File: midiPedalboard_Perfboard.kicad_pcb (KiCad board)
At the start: 4 copper layers, 66 x 50.8 mm, 53 parts, among them J1 wire, J10 wire, J11 wire, J12 wire, J13 wire, J14 wire, J15 MIDI_4, J16 MIDI_5, J17 MIDI_4, J18 MIDI_2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

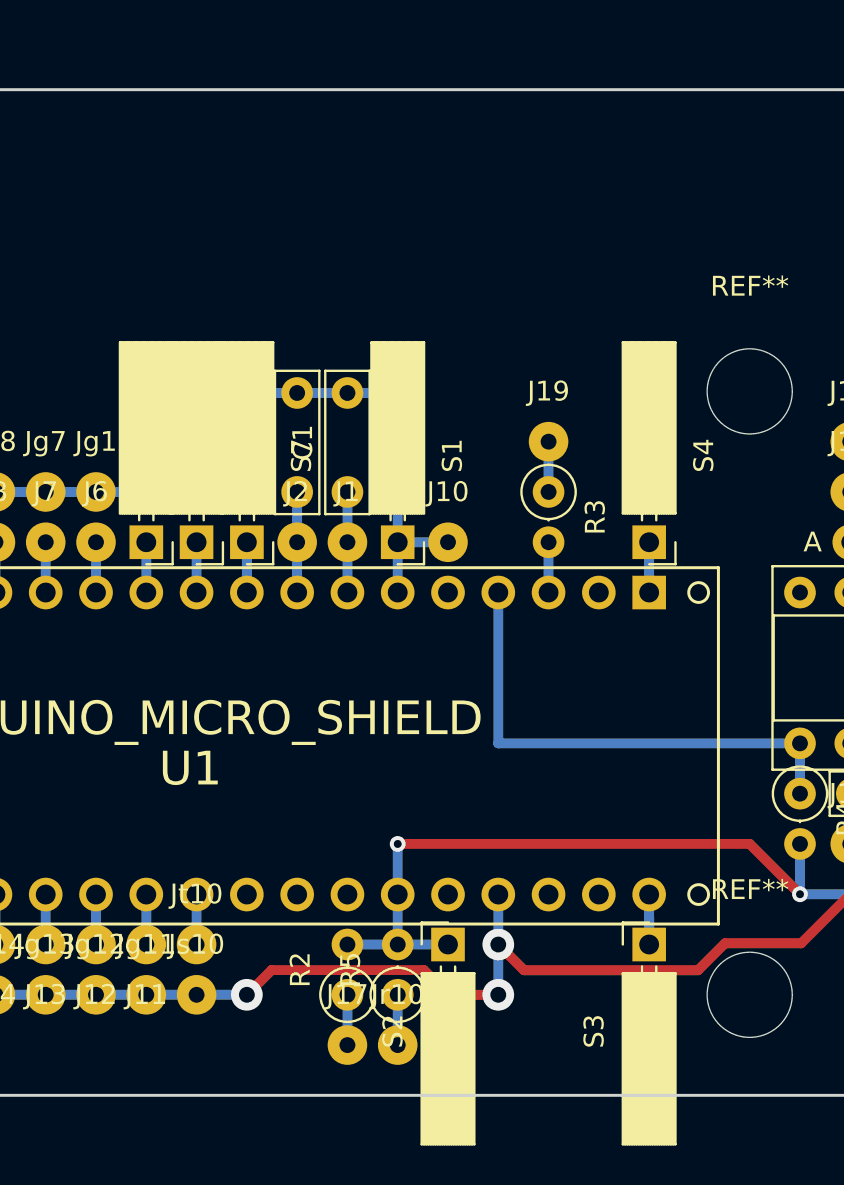
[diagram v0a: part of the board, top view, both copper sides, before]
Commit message: swap screen connectors to one connectors
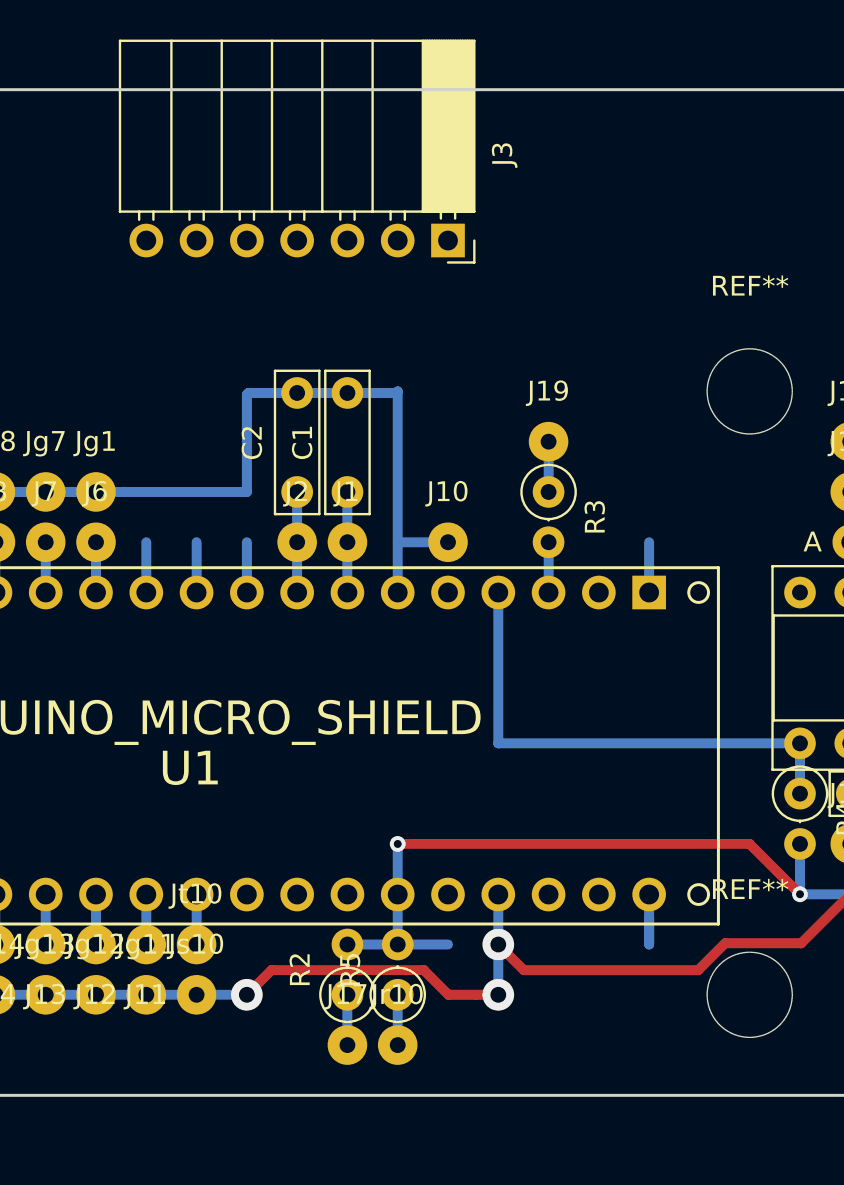
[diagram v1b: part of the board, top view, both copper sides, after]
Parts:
- removed S1, S2, S3, S4, S5, S6, S7: Socket, Connector_PinSocket_2.54mm:PinSocket_1x01_P2.54mm_Horizontal
- added J3: Screen, Connector_PinSocket_2.54mm:PinSocket_1x07_P2.54mm_Horizontal, F.Cu at (129.5, 99.1)

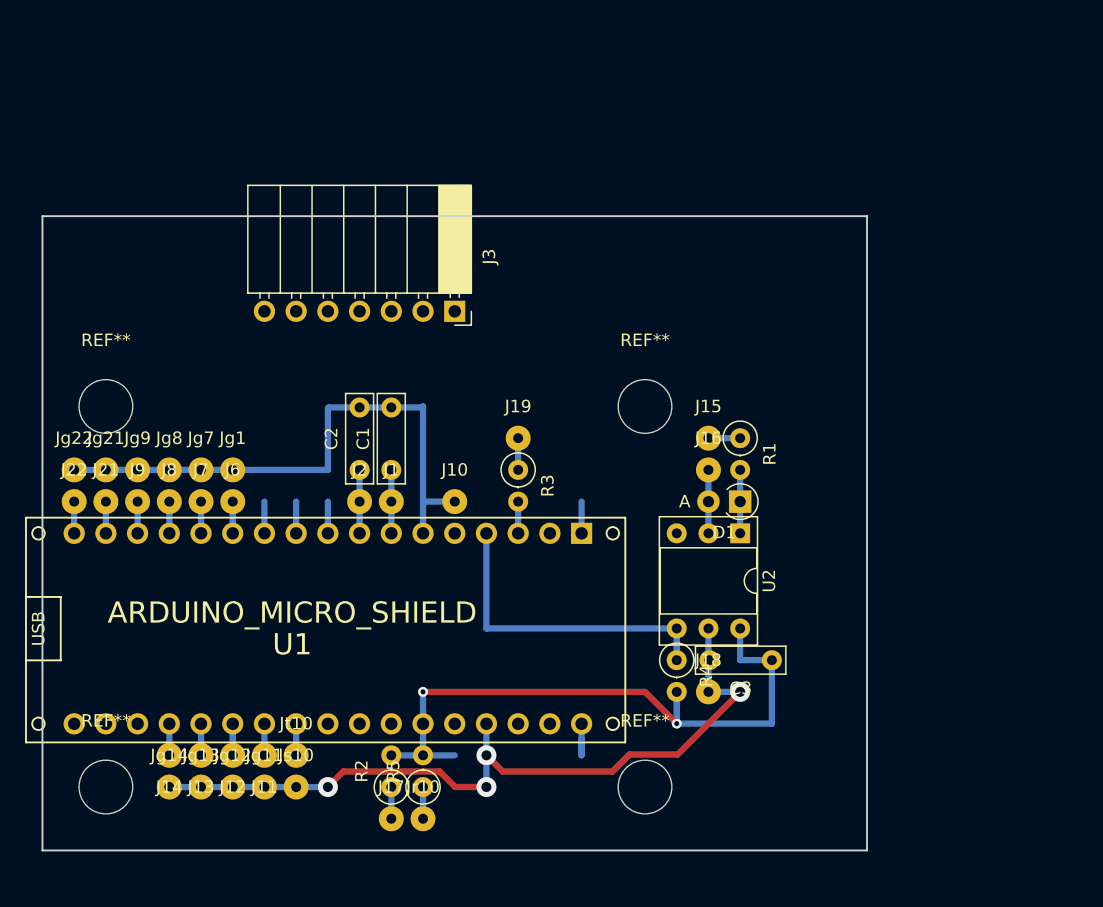
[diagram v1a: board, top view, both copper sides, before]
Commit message: move hole, connect everything
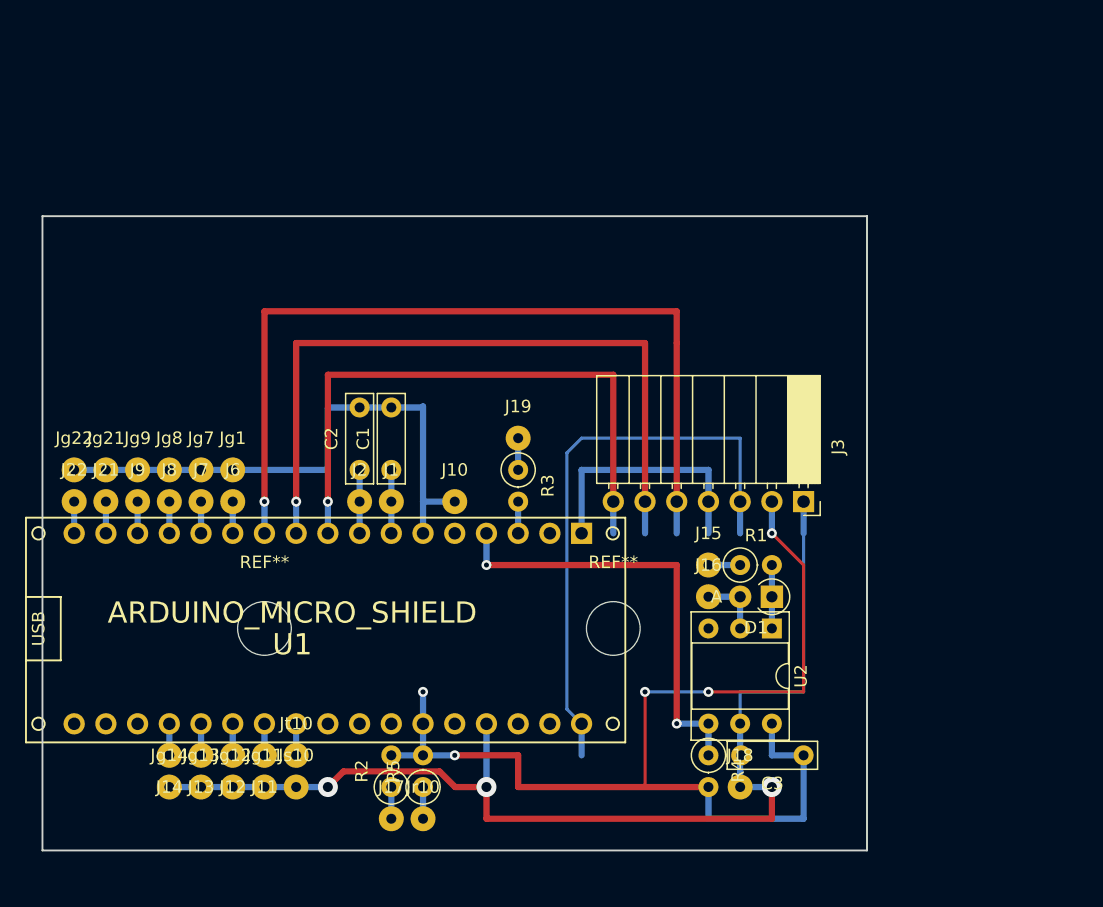
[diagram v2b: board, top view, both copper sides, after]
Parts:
- removed the REF** at (144.8, 137.2)
- removed the REF** at (144.8, 106.7)
- removed the REF** at (101.6, 137.2)
- added REF**: MountingHole_4.3mm_M4, MountingHole:MountingHole_4.3mm_M4, F.Cu at (114.3, 124.5)
- moved REF** 44.4 mm to (142.2, 124.5)
- moved J3 31.8 mm to (157.5, 114.3)
- moved J15 10.2 mm to (149.9, 119.4)
- moved J16 10.2 mm to (149.9, 121.9)
- moved R1 10.2 mm to (152.4, 119.4), turned to 0 degrees
- moved R4 8.03 mm to (149.9, 134.6)
- moved C3 8.03 mm to (157.5, 134.6)
- moved D1 8.03 mm to (154.9, 121.9)
- moved J18 8.03 mm to (152.4, 137.2)
- moved U2 8.03 mm to (154.9, 124.5)
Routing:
- net /screen_res: track 2.54 -> 68.6 mm, vias 0 -> 1
- net /screen_dc: track 2.54 -> 58.4 mm, vias 0 -> 1
- net /screen_cs: track 2.54 -> 48.3 mm, vias 0 -> 1
- net /screen_sck: track 3.87 -> 46.7 mm
- net VCC: track 51.9 -> 90.0 mm, vias 2 -> 5
- net GND: track 125.6 -> 152.9 mm, vias 4 -> 3
- net /screen_sda: track 2.54 -> 20.3 mm
- net /UART_RX: track 25.4 -> 35.6 mm, vias 0 -> 2

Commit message: add a second exp pedal input
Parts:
- added Jr11: wire, Connector_Wire:SolderWirePad_1x01_Drill0.8mm, F.Cu at (121.9, 139.7)
- added Js11: wire, Connector_Wire:SolderWirePad_1x01_Drill0.8mm, F.Cu at (119.4, 137.2)
- added Jt11: wire, Connector_Wire:SolderWirePad_1x01_Drill0.8mm, F.Cu at (119.4, 134.6)
- added R6: 100, Resistor_THT:R_Axial_DIN0207_L6.3mm_D2.5mm_P2.54mm_Vertical, F.Cu at (121.9, 137.2)
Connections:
- U1 pad A5: Net-(U1-PadA5) -> /exp_2
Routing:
- net GND: track 152.9 -> 156.1 mm
- net VCC: track 90.0 -> 92.5 mm
- net Net-(Jr11-Pad1): track 0.00 -> 2.54 mm
- net /exp_2: track 0.00 -> 2.52 mm

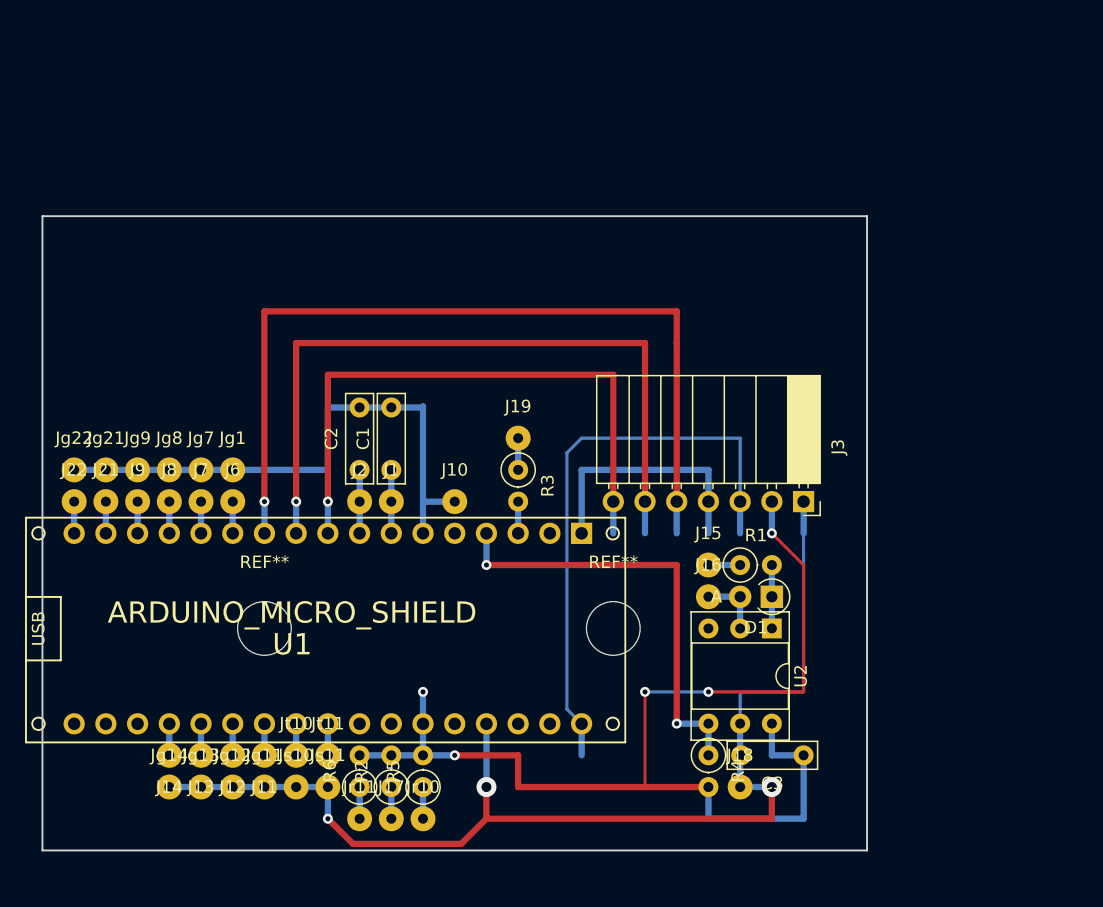
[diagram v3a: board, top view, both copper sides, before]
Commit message: some placment and connection
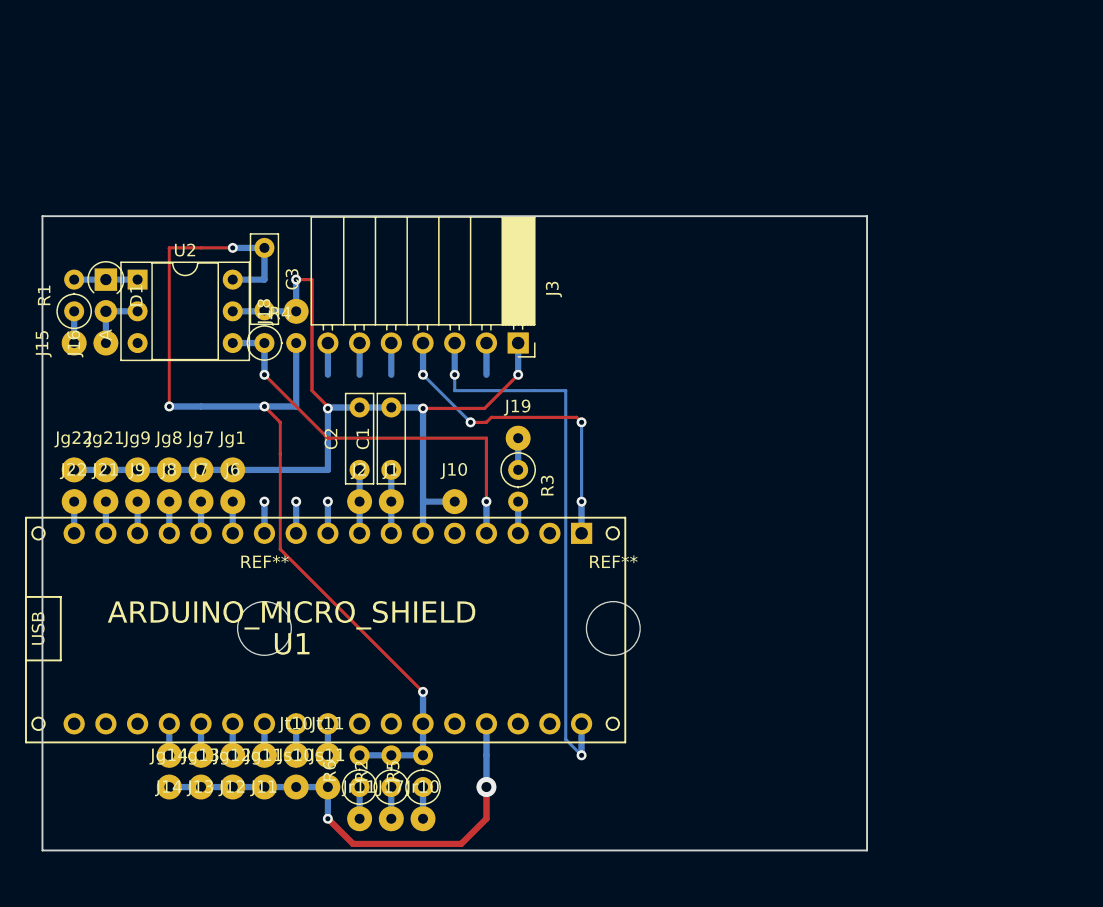
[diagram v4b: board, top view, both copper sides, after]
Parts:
- moved C3 59.3 mm to (114.3, 94.0), turned to 270 degrees
- moved D1 59.1 mm to (101.6, 96.5), turned to 270 degrees
- moved U2 58.0 mm to (104.1, 96.5), turned to 0 degrees
- moved R1 57.1 mm to (99.1, 99.1), turned to 90 degrees
- moved J15 53.8 mm to (99.1, 101.6), turned to 90 degrees
- moved J16 52.4 mm to (101.6, 101.6), turned to 90 degrees
- moved J18 52.1 mm to (116.8, 99.1), turned to 90 degrees
- moved R4 48.5 mm to (114.3, 101.6), turned to 0 degrees
- moved J3 26.2 mm to (134.6, 101.6)
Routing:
- net /screen_res: track 68.6 -> 5.08 mm
- net /screen_dc: track 58.4 -> 5.08 mm
- net /screen_cs: track 48.3 -> 5.08 mm
- net GND: track 156.1 -> 131.1 mm, vias 3 -> 6
- net VCC: track 92.5 -> 81.5 mm, vias 5 -> 4
- net /screen_sda: track 20.3 -> 26.0 mm, vias 0 -> 4
- net /UART_RX: track 35.6 -> 32.6 mm
- net /screen_sck: track 46.7 -> 45.0 mm, vias 0 -> 2

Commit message: rotate the design
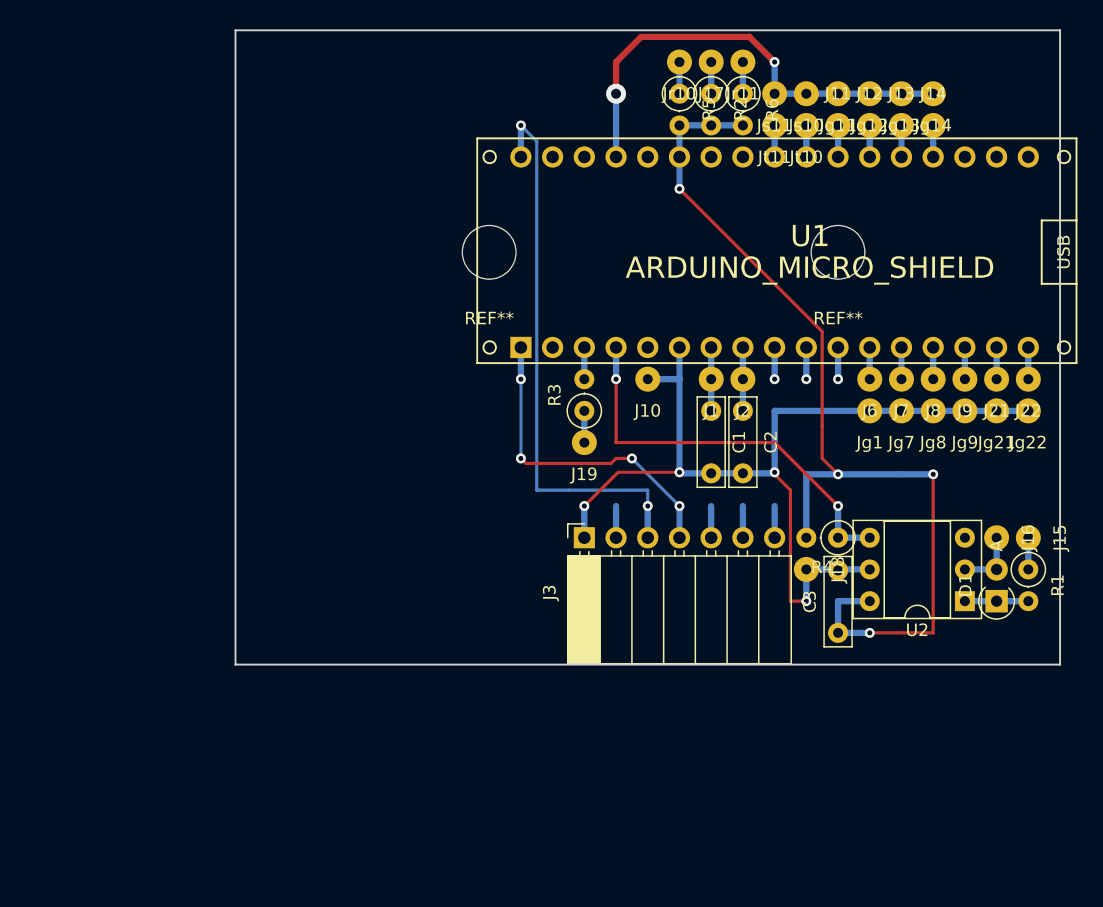
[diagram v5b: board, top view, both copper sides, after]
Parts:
- moved Jg14 82.6 mm to (167.9, 81.6), turned to 180 degrees
- moved J14 79.3 mm to (167.9, 84.2), turned to 180 degrees
- moved R1 79.2 mm to (175.5, 119.7), turned to 270 degrees
- moved Jg13 78.9 mm to (165.3, 81.6), turned to 180 degrees
- moved J15 78.0 mm to (175.5, 117.2), turned to 270 degrees
- moved J22 77.0 mm to (175.5, 104.5), turned to 180 degrees
- moved Jg22 76.6 mm to (175.5, 107.0), turned to 180 degrees
- moved D1 75.8 mm to (172.9, 122.3), turned to 90 degrees
- moved J13 75.4 mm to (165.3, 84.2), turned to 180 degrees
- moved Jg12 75.4 mm to (162.8, 81.6), turned to 180 degrees
- moved J16 73.0 mm to (172.9, 117.2), turned to 270 degrees
- moved Jg11 72.1 mm to (160.2, 81.6), turned to 180 degrees
- moved J21 72.0 mm to (172.9, 104.5), turned to 180 degrees
- moved J12 71.7 mm to (162.8, 84.2), turned to 180 degrees
- moved Jg21 71.5 mm to (172.9, 107.0), turned to 180 degrees
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
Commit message: relayout and connection
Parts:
- moved J17 45.5 mm to (134.6, 121.9)
- moved R2 40.8 mm to (134.6, 119.4), turned to 90 degrees
- moved J18 18.7 mm to (147.3, 104.1)
- moved J10 16.7 mm to (160.0, 111.8)
- moved C1 12.5 mm to (162.6, 106.7)
- moved J1 12.5 mm to (162.6, 104.1)
- moved C2 12.5 mm to (165.1, 106.7)
- moved J2 12.5 mm to (165.1, 104.1)
- moved REF** 9.94 mm to (142.2, 94.3)
- moved REF** 7.41 mm to (167.6, 94.0)
- moved J3 5.44 mm to (139.7, 111.8)
- moved J6 5.31 mm to (157.5, 104.1)
- moved Jg1 5.31 mm to (157.5, 106.7)
- moved J7 5.31 mm to (160.0, 104.1)
- moved Jg7 5.31 mm to (160.0, 106.7)
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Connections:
- U1 pad 2: /rotary_a -> /screen_res
- U1 pad 3: /rotary_b -> /screen_dc
- U1 pad 5: /screen_dc -> /btn_ok
- U1 pad 6: /screen_res -> /btn_cancel
- U1 pad 7: /btn_ok -> /rotary_a
- U1 pad 8: /btn_cancel -> /rotary_b
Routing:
- net VCC: track 81.5 -> 129.4 mm, vias 4 -> 6
- net GND: track 131.1 -> 142.5 mm, vias 6 -> 5
- net /screen_sda: track 26.0 -> 19.9 mm, vias 4 -> 2
- net /screen_res: track 5.08 -> 10.2 mm, vias 1 -> 2
- net /screen_dc: track 5.08 -> 10.2 mm, vias 1 -> 2
- net /screen_cs: track 5.08 -> 10.2 mm, vias 1 -> 2
- net /UART_RX: track 32.6 -> 35.9 mm
- net /screen_sck: track 45.0 -> 46.0 mm
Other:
- copper layers 4 -> 8
